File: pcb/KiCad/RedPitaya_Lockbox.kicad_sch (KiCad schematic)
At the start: 22 parts, among them J1 C64AC

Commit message: Set symbols and mounting holes to DNF.
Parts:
- H1, H2, LOGO1, LOGO2, LOGO3: Config (none) -> DNF
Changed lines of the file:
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@@
+      (effects (font (size 1.27 1.27)) hide)
+    )
+    (property "Config" "DNF" (id 4) (at 243.84 171.45 0)
       (effects (font (size 1.27 1.27)) hide)
     )
@@
       (effects (font (size 1.27 1.27)) hide)
     )
+    (property "Config" "DNF" (id 4) (at 276.86 173.99 0)
+      (effects (font (size 1.27 1.27)) hide)
+    )
   )
   (symbol (lib_id "Mechanical:MountingHole") (at 265.43 133.35 0) (unit 1)
@@
     )
     (property "Datasheet" "~" (id 3) (at 265.43 133.35 0)
+      (effects (font (size 1.27 1.27)) hide)
+    )
+    (property "Config" "DNF" (id 4) (at 265.43 133.35 0)
       (effects (font (size 1.27 1.27)) hide)
     )
@@
       (effects (font (size 1.27 1.27)) hide)
     )
+    (property "Config" "DNF" (id 4) (at 265.43 138.43 0)
+      (effects (font (size 1.27 1.27)) hide)
+    )
   )
   (symbol (lib_id "Custom_logos:Logo_ROHS") (at 223.52 171.45 0) (unit 1)
@@
       (effects (font (size 1.27 1.27)) hide)
     )
+    (property "Config" "DNF" (id 4) (at 223.52 171.45 0)
+      (effects (font (size 1.27 1.27)) hide)
+    )

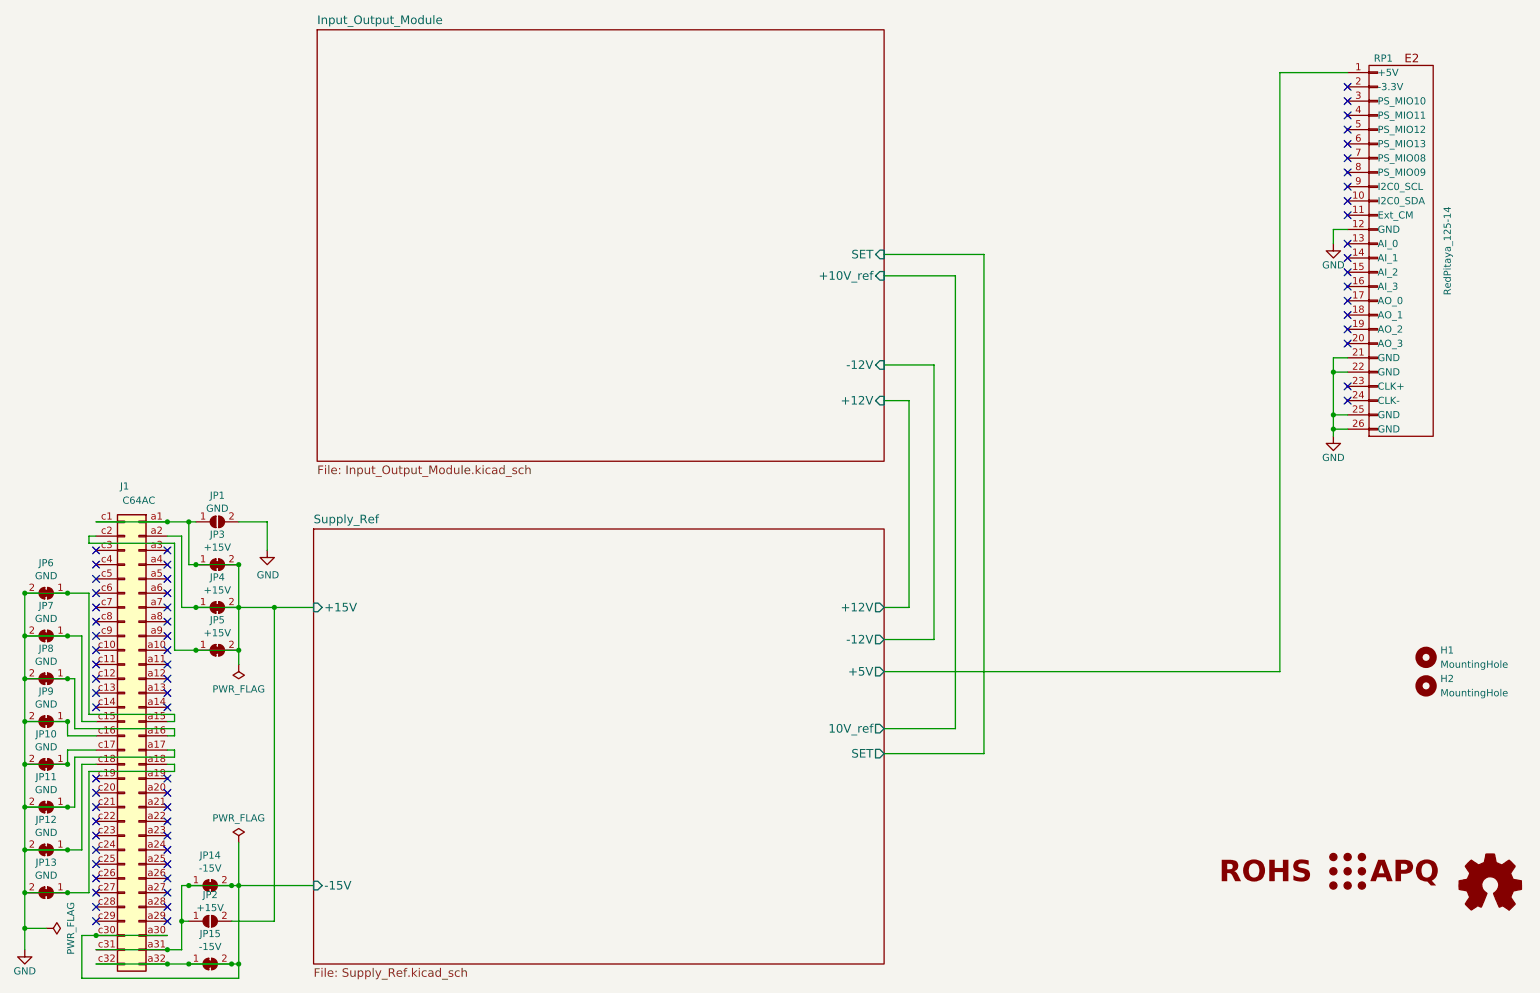
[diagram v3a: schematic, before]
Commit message: Updated to KiCAD 7 Cleaned up schematics Updated footprints Cleaned up PCB
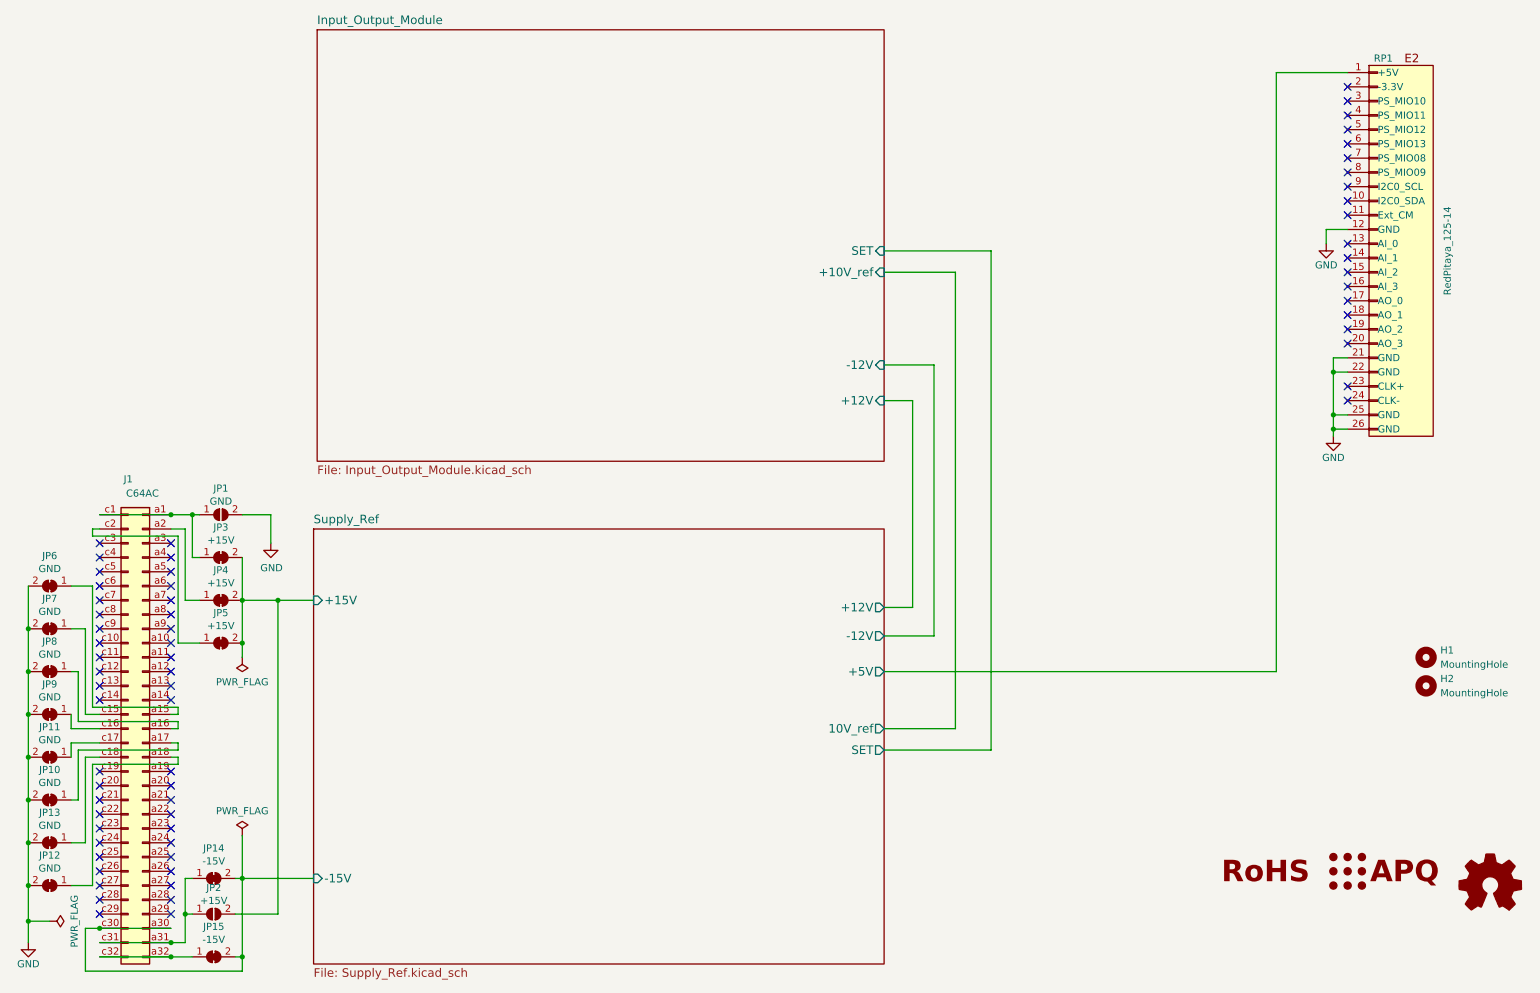
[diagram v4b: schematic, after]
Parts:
- JP10, JP11, JP12, JP13, JP14, JP15, JP3, JP4, JP5, JP6, JP7, JP8, JP9: footprint Jumper:SolderJumper-2_P1.3mm_Open_RoundedPad1.0x1.5mm -> Jumper:SolderJumper-2_P1.3mm_Bridged_RoundedPad1.0x1.5mm
- LOGO1: now left out of the parts list
- LOGO3: value Logo_ROHS -> Logo_RoHS; symbol Custom_logos:Logo_ROHS -> Custom_logos:Logo_RoHS
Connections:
- net GND: no longer J1.a15 (Pin_a15), J1.a16 (Pin_a16), J1.a17 (Pin_a17), J1.a18 (Pin_a18), J1.c15 (Pin_c15), J1.c16 (Pin_c16), J1.c17 (Pin_c17), J1.c18 (Pin_c18), JP10.1 (A), JP11.1 (A), JP12.1 (A), JP13.1 (A), JP6.1 (A), JP7.1 (A), JP8.1 (A), JP9.1 (A)
- net Supply_Ref/+15V: no longer J1.a1 (Pin_a1), J1.a2 (Pin_a2), J1.c1 (Pin_c1), J1.c2 (Pin_c2), JP1.1 (A), JP3.1 (A), JP4.1 (A), JP5.1 (A)
- net Supply_Ref/-15V: no longer J1.a31 (Pin_a31), J1.a32 (Pin_a32), J1.c31 (Pin_c31), J1.c32 (Pin_c32), JP14.1 (A), JP15.1 (A), JP2.1 (A)
- new net: J1.a1 (Pin_a1), J1.c1 (Pin_c1), JP1.1 (A), JP3.1 (A)
- new net: J1.a15 (Pin_a15), JP6.1 (A)
- new net: J1.a16 (Pin_a16), JP8.1 (A)
- new net: J1.a17 (Pin_a17), JP10.1 (A)
- new net: J1.a18 (Pin_a18), JP12.1 (A)
- new net: J1.a2 (Pin_a2), JP4.1 (A)
- new net: J1.a31 (Pin_a31), J1.c31 (Pin_c31), JP14.1 (A), JP2.1 (A)
- new net: J1.a32 (Pin_a32), J1.c32 (Pin_c32), JP15.1 (A)
- new net: J1.c15 (Pin_c15), JP7.1 (A)
- new net: J1.c16 (Pin_c16), JP9.1 (A)
- new net: J1.c17 (Pin_c17), JP11.1 (A)
- new net: J1.c18 (Pin_c18), JP13.1 (A)
- new net: J1.c2 (Pin_c2), JP5.1 (A)
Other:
- moved on the sheet: J1, JP1, JP10, JP11, JP12, JP13, JP14, JP15, JP2, JP3, JP4, JP5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

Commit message: Prepare release of v1.6.2
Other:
- moved on the sheet: JP14, JP2
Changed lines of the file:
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@@
   (title_block
     (title "RedPitaya Lockbox")
-    (date "2023-08-08")
-    (rev "1.6.1")
+    (date "2023-11-03")
+    (rev "1.6.2")
     (company "Atoms-Photons-Quanta, Institut für Angewandte Physik, TU Darmstadt")
     (comment 1 "Tilman Preuschoff")
@@
   (junction (at 16.51 151.13) (diameter 0) (color 0 0 0 0)
   )
+  (junction (at 44.45 177.8) (diameter 0) (color 0 0 0 0)
+  )
   (junction (at 248.92 92.71) (diameter 0) (color 0 0 0 0)
   )
@@
   (junction (at 248.92 82.55) (diameter 0) (color 0 0 0 0)
   )
-  (junction (at 44.45 179.07) (diameter 0) (color 0 0 0 0)
+  (junction (at 54.61 170.18) (diameter 0) (color 0 0 0 0)
   )
   (junction (at 41.91 186.69) (diameter 0) (color 0 0 0 0)
@@
   )
   (junction (at 16.51 173.99) (diameter 0) (color 0 0 0 0)
-  )
-  (junction (at 54.61 172.72) (diameter 0) (color 0 0 0 0)
   )
   (no_connect (at 251.46 52.07))
@@
   (no_connect (at 29.21 115.57))
   (no_connect (at 41.91 115.57))
-  (wire (pts (xy 44.45 184.15) (xy 44.45 179.07))
-    (stroke (width 0) (type default))
-  )
   (wire (pts (xy 54.61 115.57) (xy 54.61 123.19))
     (stroke (width 0) (type default))
@@
     (stroke (width 0) (type default))
   )
-  (wire (pts (xy 44.45 172.72) (xy 44.45 179.07))
+  (wire (pts (xy 44.45 170.18) (xy 44.45 177.8))
     (stroke (width 0) (type default))
   )
@@
     (stroke (width 0) (type default))
   )
-  (wire (pts (xy 45.72 172.72) (xy 44.45 172.72))
+  (wire (pts (xy 45.72 170.18) (xy 44.45 170.18))
     (stroke (width 0) (type default))
   )
@@
     (stroke (width 0) (type default))
   )
-  (wire (pts (xy 53.34 179.07) (xy 60.96 179.07))
+  (wire (pts (xy 53.34 177.8) (xy 60.96 177.8))
     (stroke (width 0) (type default))
   )
@@
     (stroke (width 0) (type default))
   )
+  (wire (pts (xy 44.45 177.8) (xy 44.45 184.15))
+    (stroke (width 0) (type default))
+  )
   (wire (pts (xy 181.61 146.05) (xy 181.61 64.77))
     (stroke (width 0) (type default))
@@
     (stroke (width 0) (type default))
   )
-  (wire (pts (xy 54.61 172.72) (xy 67.31 172.72))
+  (wire (pts (xy 54.61 170.18) (xy 67.31 170.18))
     (stroke (width 0) (type default))
   )
@@
     (stroke (width 0) (type default))
   )
-  (wire (pts (xy 54.61 172.72) (xy 53.34 172.72))
+  (wire (pts (xy 54.61 170.18) (xy 53.34 170.18))
     (stroke (width 0) (type default))
   )
@@
     (stroke (width 0) (type default))
   )
-  (wire (pts (xy 54.61 165.1) (xy 54.61 172.72))
+  (wire (pts (xy 54.61 165.1) (xy 54.61 170.18))
     (stroke (width 0) (type default))
   )
@@
     (stroke (width 0) (type default))
   )
-  (wire (pts (xy 44.45 179.07) (xy 45.72 179.07))
-    (stroke (width 0) (type default))
-  )
-  (wire (pts (xy 54.61 172.72) (xy 54.61 186.69))
+  (wire (pts (xy 44.45 177.8) (xy 45.72 177.8))
+    (stroke (width 0) (type default))
+  )
+  (wire (pts (xy 54.61 170.18) (xy 54.61 186.69))
     (stroke (width 0) (type default))
   )
@@
     (stroke (width 0) (type default))
   )
-  (wire (pts (xy 60.96 179.07) (xy 60.96 123.19))
+  (wire (pts (xy 60.96 177.8) (xy 60.96 123.19))
     (stroke (width 0) (type default))
   )
@@
     )
   )
-  (symbol (lib_id "Jumper:SolderJumper_2_Bridged") (at 49.53 172.72 0) (unit 1)
-    (in_bom yes) (on_board yes) (dnp no)
-    (property "Reference" "JP14" (at 49.53 167.3352 0)
-      (effects (font (size 1.27 1.27)))
-    )
-    (property "Value" "-15V" (at 49.53 169.6466 0)
-      (effects (font (size 1.27 1.27)))
-    )
-    (property "Footprint" "Jumper:SolderJumper-2_P1.3mm_Bridged_RoundedPad1.0x1.5mm" (at 49.53 172.72 0)
-      (effects (font (size 1.27 1.27)) hide)
-    )
-    (property "Datasheet" "~" (at 49.53 172.72 0)
-      (effects (font (size 1.27 1.27)) hide)
-    )
-    (property "Config" "DNF" (at 49.53 172.72 0)
-      (effects (font (size 1.27 1.27)) hide)
-    )
-    (property "MFN" "" (at 49.53 172.72 0)
-      (effects (font (size 1.27 1.27)) hide)
-    )
-    (property "PN" "" (at 49.53 172.72 0)
+  (symbol (lib_id "Jumper:SolderJumper_2_Bridged") (at 49.53 170.18 0) (unit 1)
+    (in_bom yes) (on_board yes) (dnp no)
+    (property "Reference" "JP14" (at 49.53 164.7952 0)
+      (effects (font (size 1.27 1.27)))
+    )
+    (property "Value" "-15V" (at 49.53 167.1066 0)
+      (effects (font (size 1.27 1.27)))
+    )
+    (property "Footprint" "Jumper:SolderJumper-2_P1.3mm_Bridged_RoundedPad1.0x1.5mm" (at 49.53 170.18 0)
+      (effects (font (size 1.27 1.27)) hide)
+    )
+    (property "Datasheet" "~" (at 49.53 170.18 0)
+      (effects (font (size 1.27 1.27)) hide)
+    )
+    (property "Config" "DNF" (at 49.53 170.18 0)
+      (effects (font (size 1.27 1.27)) hide)
+    )
+    (property "MFN" "" (at 49.53 170.18 0)
+      (effects (font (size 1.27 1.27)) hide)
+    )
+    (property "PN" "" (at 49.53 170.18 0)
       (effects (font (size 1.27 1.27)) hide)
     )
@@
     )
   )
-  (symbol (lib_id "Jumper:SolderJumper_2_Open") (at 49.53 179.07 0) (unit 1)
-    (in_bom yes) (on_board yes) (dnp no)
-    (property "Reference" "JP2" (at 49.53 174.371 0)
-      (effects (font (size 1.27 1.27)))
-    )
-    (property "Value" "+15V" (at 49.53 176.6824 0)
-      (effects (font (size 1.27 1.27)))
-    )
-    (property "Footprint" "Jumper:SolderJumper-2_P1.3mm_Open_RoundedPad1.0x1.5mm" (at 49.53 179.07 0)
-      (effects (font (size 1.27 1.27)) hide)
-    )
-    (property "Datasheet" "~" (at 49.53 179.07 0)
-      (effects (font (size 1.27 1.27)) hide)
-    )
-    (property "Config" "DNF" (at 49.53 179.07 0)
+  (symbol (lib_id "Jumper:SolderJumper_2_Open") (at 49.53 177.8 0) (unit 1)
+    (in_bom yes) (on_board yes) (dnp no)
+    (property "Reference" "JP2" (at 49.53 173.101 0)
+      (effects (font (size 1.27 1.27)))
+    )
+    (property "Value" "+15V" (at 49.53 175.4124 0)
+      (effects (font (size 1.27 1.27)))
+    )
+    (property "Footprint" "Jumper:SolderJumper-2_P1.3mm_Open_RoundedPad1.0x1.5mm" (at 49.53 177.8 0)
+      (effects (font (size 1.27 1.27)) hide)
+    )
+    (property "Datasheet" "~" (at 49.53 177.8 0)
+      (effects (font (size 1.27 1.27)) hide)
+    )
+    (property "Config" "DNF" (at 49.53 177.8 0)
       (effects (font (size 1.27 1.27)) hide)
     )
@@
       (effects (font (size 1.524 1.524)) (justify left top))
     )
-    (pin "-15V" input (at 67.31 172.72 180)
+    (pin "-15V" input (at 67.31 170.18 180)
       (effects (font (size 1.524 1.524)) (justify left))
     )

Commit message: Fixed logos in the schematic
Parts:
- LOGO1: Config DNF -> (none)
- LOGO2, LOGO3: Config DNF -> (none); now left out of the parts list
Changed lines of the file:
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@@
-      (effects (font (size 1.27 1.27)) hide)
-    )
-    (property "Config" "DNF" (at 243.84 171.45 0)
       (effects (font (size 1.27 1.27)) hide)
     )
@@
   )
   (symbol (lib_id "Graphic:Logo_Open_Hardware_Small") (at 276.86 173.99 0) (unit 1)
-    (in_bom yes) (on_board yes) (dnp no)
+    (in_bom no) (on_board yes) (dnp no)
     (property "Reference" "LOGO2" (at 276.86 167.005 0)
       (effects (font (size 1.27 1.27)) hide)
@@
       (effects (font (size 1.27 1.27)) hide)
     )
-    (property "Config" "DNF" (at 276.86 173.99 0)
+    (property "Sim.Enable" "0" (at 276.86 173.99 0)
       (effects (font (size 1.27 1.27)) hide)
     )
-    (property "Sim.Enable" "0" (at 276.86 173.99 0)
+    (property "MFN" "" (at 276.86 173.99 0)
+      (effects (font (size 1.27 1.27)) hide)
+    )
+    (property "PN" "" (at 276.86 173.99 0)
       (effects (font (size 1.27 1.27)) hide)
     )
@@
   )
   (symbol (lib_id "Custom_logos:Logo_RoHS") (at 223.52 171.45 0) (unit 1)
-    (in_bom yes) (on_board yes) (dnp no)
+    (in_bom no) (on_board yes) (dnp no)
     (property "Reference" "LOGO3" (at 229.87 164.465 0)
       (effects (font (size 1.27 1.27)) hide)
@@
       (effects (font (size 1.27 1.27)) hide)
     )
-    (property "Config" "DNF" (at 223.52 171.45 0)
-      (effects (font (size 1.27 1.27)) hide)
-    )

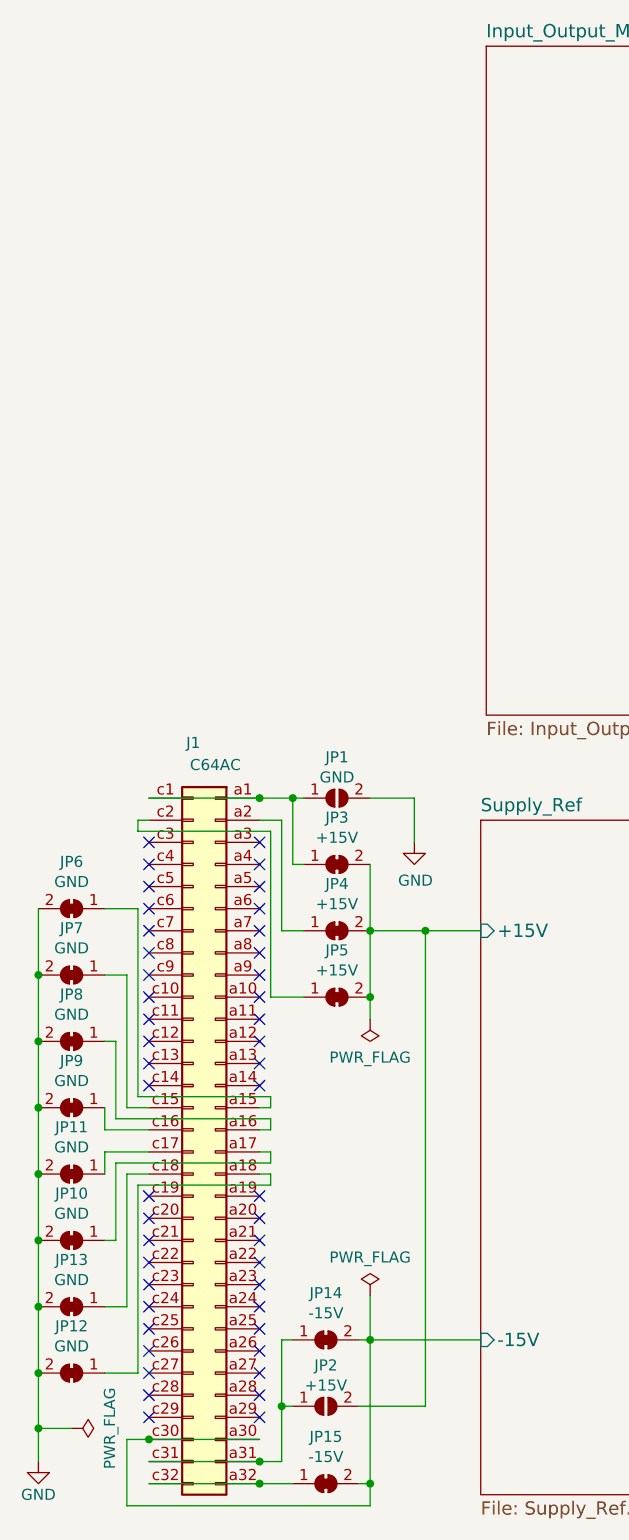
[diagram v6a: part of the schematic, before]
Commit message: Updated to KiCad 8
Added assembly instructions for the potentiometer
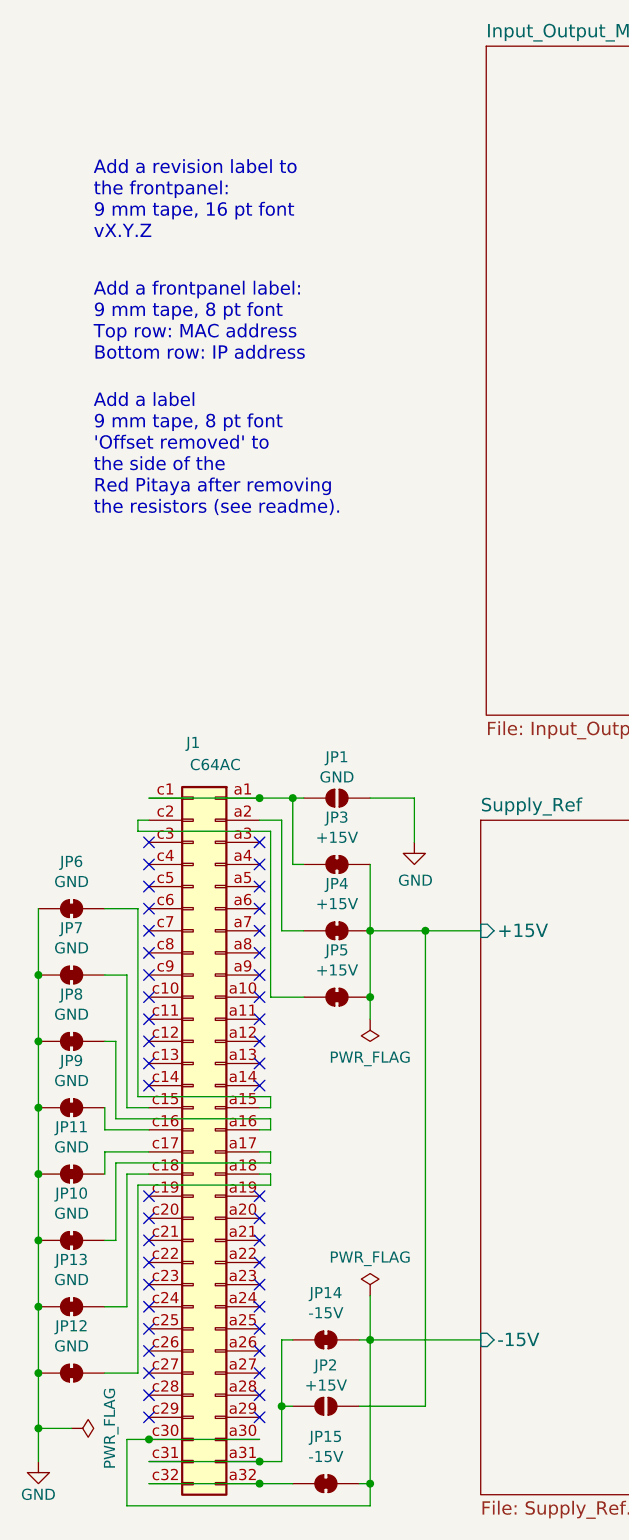
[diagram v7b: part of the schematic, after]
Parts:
- H1, H2, JP1, JP10, JP11, JP12, JP13, JP14, JP15, JP2, JP3, JP4, JP5, JP6, JP7, JP8, JP9: now left out of the parts list
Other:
- note added: "Add a frontpanel label: 9 mm tape, 8 pt font Top row: MAC address Bottom row: IP address"
- note added: "Add a label 9 mm tape, 8 pt font 'Offset removed' to the side of the Red Pitaya after removing the resistors (see readme)."
- note added: "Add a revision label to the frontpanel: 9 mm tape, 16 pt font vX.Y.Z"
